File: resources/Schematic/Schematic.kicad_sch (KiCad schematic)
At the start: 5 parts

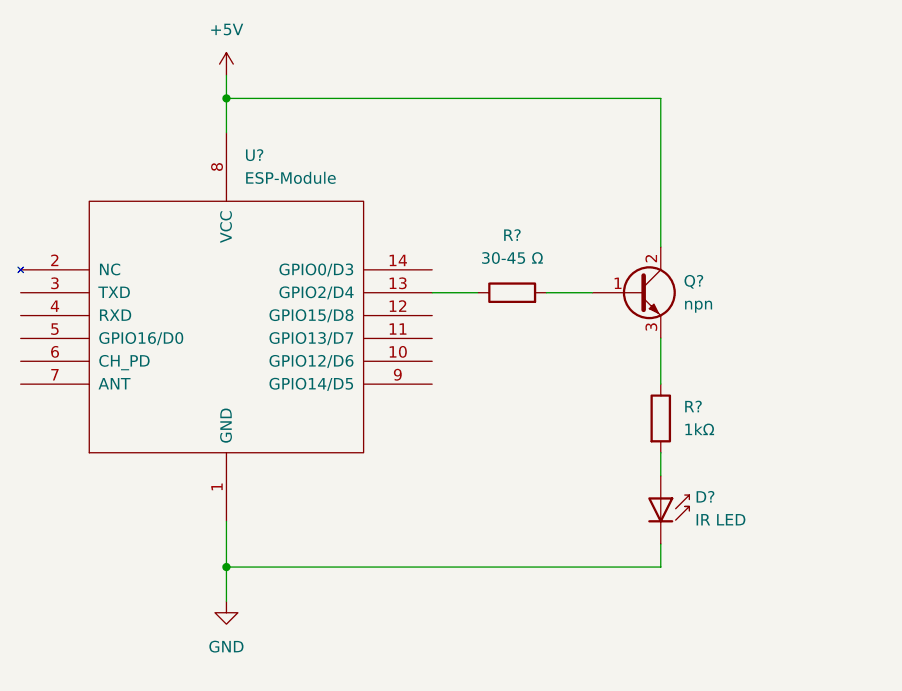
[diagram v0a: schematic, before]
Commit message: update schematic
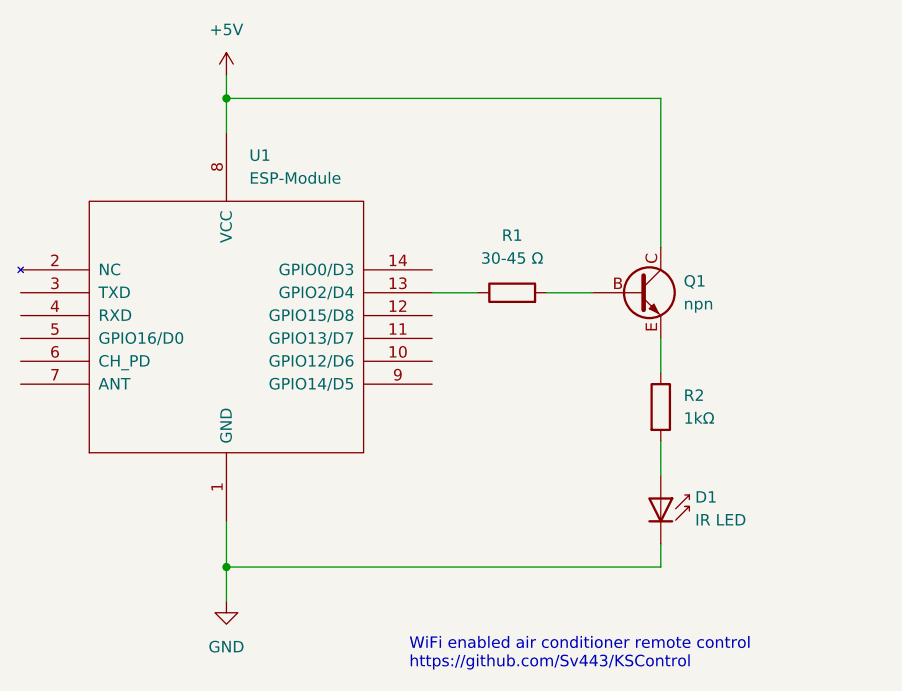
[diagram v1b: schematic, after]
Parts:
- gave numbers to parts that had none: 5
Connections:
- net +5V: now also Q1.C; no longer Q1.2 (C)
- net at R1.2: now also Q1.B; no longer Q1.1 (B)
- net at R2.1: now also Q1.E; no longer Q1.3 (E)
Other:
- note added: "WiFi enabled air conditioner remote control https://github.com/Sv443/KSControl"
- moved on the sheet: R2
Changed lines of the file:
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@@
     (stroke (width 0) (type default) (color 0 0 0 0))
   )
-  (wire (pts (xy 82.55 39.37) (xy 82.55 44.45))
+  (wire (pts (xy 82.55 39.37) (xy 82.55 43.18))
     (stroke (width 0) (type default) (color 0 0 0 0))
   )
-  (wire (pts (xy 82.55 52.07) (xy 82.55 54.61))
+  (wire (pts (xy 82.55 50.8) (xy 82.55 54.61))
     (stroke (width 0) (type default) (color 0 0 0 0))
   )
@@
     (stroke (width 0) (type default) (color 0 0 0 0))
   )
+  (text "WiFi enabled air conditioner remote control\nhttps://github.com/Sv443/KSControl"
+    (at 54.61 76.2 0)
+    (effects (font (size 1.27 1.27)) (justify left bottom))
+  )
   (symbol (lib_id "ESP8266:ESP-03") (at 34.29 39.37 0) (unit 1)
-    (in_bom yes) (on_board yes) (fields_autoplaced)
-    (property "Reference" "U?" (id 0) (at 36.3094 19.05 0)
+    (in_bom yes) (on_board yes)
+    (property "Reference" "U1" (id 0) (at 36.83 19.05 0)
       (effects (font (size 1.27 1.27)) (justify left))
     )
-    (property "Value" "ESP-Module" (id 1) (at 36.3094 21.59 0)
+    (property "Value" "ESP-Module" (id 1) (at 36.83 21.59 0)
       (effects (font (size 1.27 1.27)) (justify left))
     )
@@
   (symbol (lib_id "LED:IR204A") (at 82.55 57.15 270) (mirror x) (unit 1)
     (in_bom yes) (on_board yes) (fields_autoplaced)
-    (property "Reference" "D?" (id 0) (at 86.36 57.0229 90)
+    (property "Reference" "D1" (id 0) (at 86.36 57.0229 90)
       (effects (font (size 1.27 1.27)) (justify left))
     )
@@
   (symbol (lib_id "Device:Q_NPN_BCE") (at 80.01 34.29 0) (unit 1)
     (in_bom yes) (on_board yes)
-    (property "Reference" "Q?" (id 0) (at 85.09 33.0199 0)
+    (property "Reference" "Q1" (id 0) (at 85.09 33.0199 0)
       (effects (font (size 1.27 1.27)) (justify left))
     )
@@
       (effects (font (size 1.27 1.27)) hide)
     )
-    (pin "1")
-    (pin "2")
-    (pin "3")
+    (pin "B")
+    (pin "C")
+    (pin "E")
   )
-  (symbol (lib_id "Device:R") (at 82.55 48.26 0) (unit 1)
+  (symbol (lib_id "Device:R") (at 82.55 46.99 0) (unit 1)
     (in_bom yes) (on_board yes) (fields_autoplaced)
-    (property "Reference" "R?" (id 0) (at 85.09 46.9899 0)
+    (property "Reference" "R2" (id 0) (at 85.09 45.7199 0)
       (effects (font (size 1.27 1.27)) (justify left))
     )
-    (property "Value" "1kΩ" (id 1) (at 85.09 49.5299 0)
+    (property "Value" "1kΩ" (id 1) (at 85.09 48.2599 0)
       (effects (font (size 1.27 1.27)) (justify left))
     )
-    (property "Footprint" "" (id 2) (at 80.772 48.26 90)
+    (property "Footprint" "" (id 2) (at 80.772 46.99 90)
       (effects (font (size 1.27 1.27)) hide)
     )
-    (property "Datasheet" "~" (id 3) (at 82.55 48.26 0)
+    (property "Datasheet" "~" (id 3) (at 82.55 46.99 0)
       (effects (font (size 1.27 1.27)) hide)
     )
@@
   (symbol (lib_id "Device:R") (at 66.04 34.29 90) (unit 1)
     (in_bom yes) (on_board yes) (fields_autoplaced)
-    (property "Reference" "R?" (id 0) (at 66.04 27.94 90))
+    (property "Reference" "R1" (id 0) (at 66.04 27.94 90))
     (property "Value" "30-45 Ω" (id 1) (at 66.04 30.48 90))
     (property "Footprint" "" (id 2) (at 66.04 36.068 90)
@@
     )
     (path "/85c08f94-4833-4e4a-9de7-ec9d4931d658"
-      (reference "D?") (unit 1) (value "IR LED") (footprint "LED_THT:LED_D3.0mm_IRBlack")
+      (reference "D1") (unit 1) (value "IR LED") (footprint "LED_THT:LED_D3.0mm_IRBlack")
     )
     (path "/bb208367-fb66-461d-8793-abeb4e7fb190"
-      (reference "Q?") (unit 1) (value "npn") (footprint "")
+      (reference "Q1") (unit 1) (value "npn") (footprint "")
+    )
+    (path "/eb595f03-dcb2-428a-ad25-118fea5674ed"
+      (reference "R1") (unit 1) (value "30-45 Ω") (footprint "")
     )
     (path "/dd47001e-f60c-4589-b566-5ce5b425dd21"
-      (reference "R?") (unit 1) (value "1kΩ") (footprint "")
-    )
-    (path "/eb595f03-dcb2-428a-ad25-118fea5674ed"
-      (reference "R?") (unit 1) (value "30-45 Ω") (footprint "")
+      (reference "R2") (unit 1) (value "1kΩ") (footprint "")
     )
     (path "/557f197c-c3d7-4f52-8e7a-23de81123a43"
-      (reference "U?") (unit 1) (value "ESP-Module") (footprint "")
+      (reference "U1") (unit 1) (value "ESP-Module") (footprint "")
     )
   )
